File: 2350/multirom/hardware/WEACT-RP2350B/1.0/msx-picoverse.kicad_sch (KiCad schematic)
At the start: 9 parts, among them U1 WEACT-RP2350B

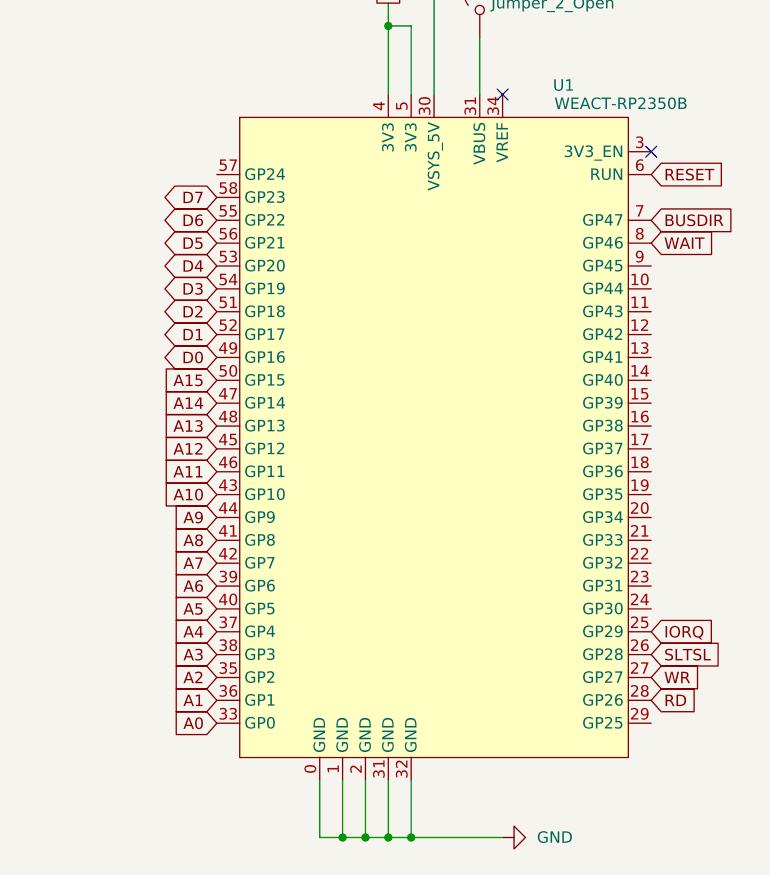
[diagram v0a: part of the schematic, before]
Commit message: loadrom and multirom ported to 2350
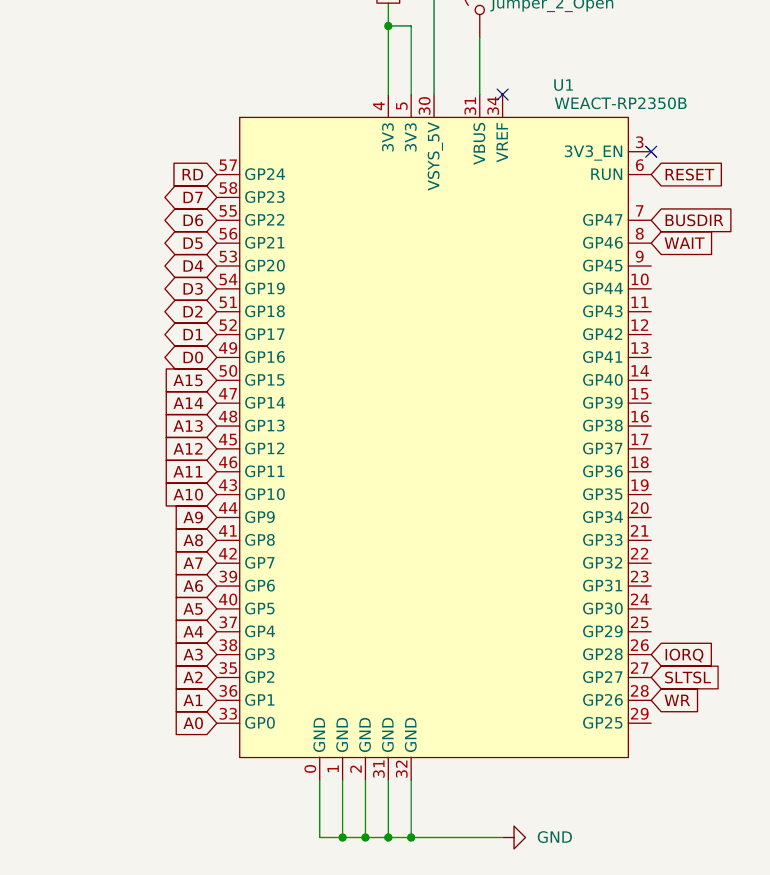
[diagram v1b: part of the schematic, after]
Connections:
- net IORQ: now also U1.26 (GP28); no longer U1.25 (GP29)
- net RD: now also U1.57 (GP24); no longer U1.28 (GP26)
- net SLTSL: now also U1.27 (GP27); no longer U1.26 (GP28)
- net WR: now also U1.28 (GP26); no longer U1.27 (GP27)

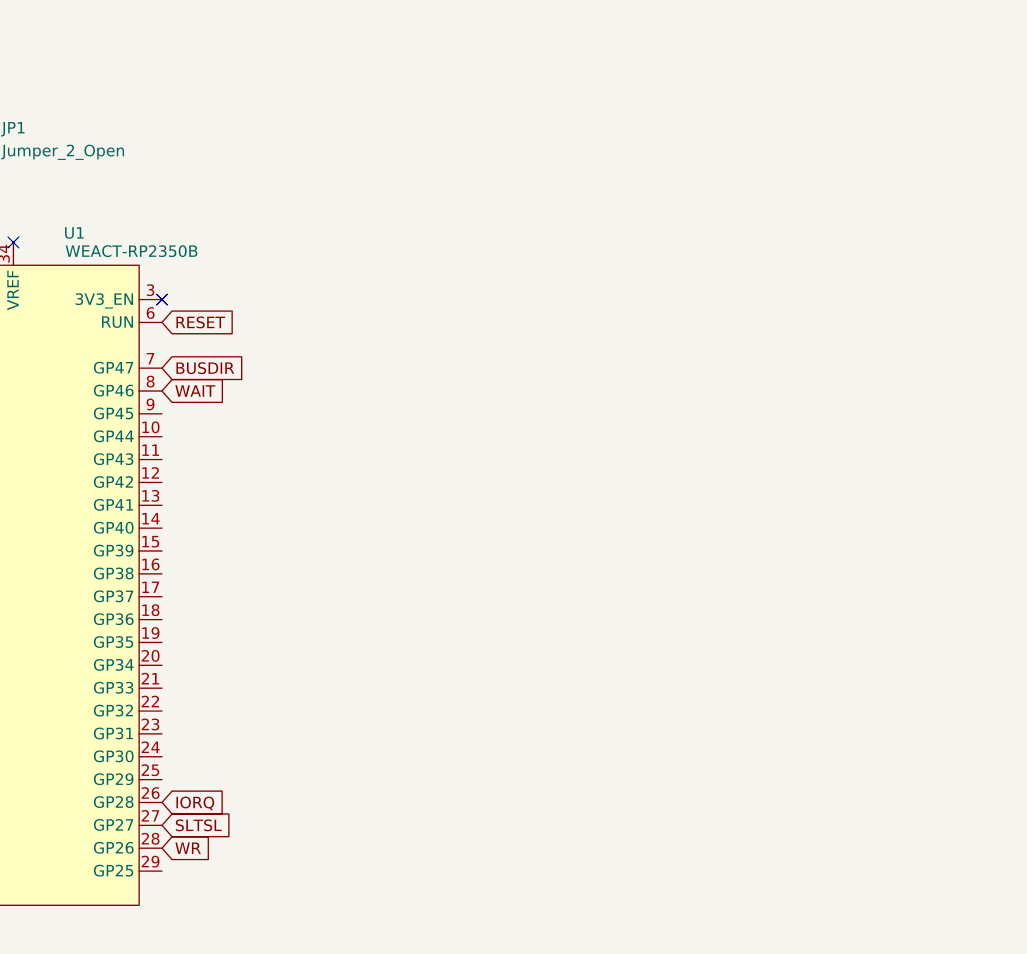
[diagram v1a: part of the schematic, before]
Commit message: connecting the microSD card
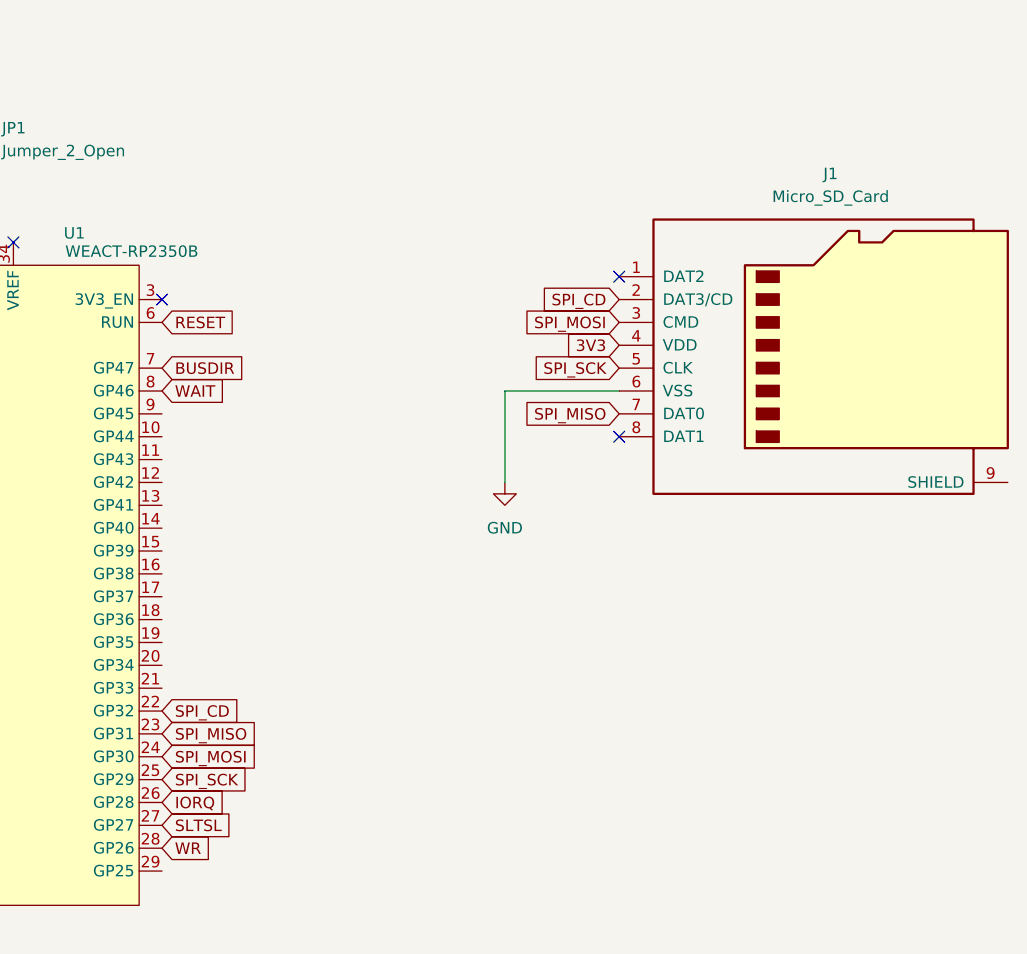
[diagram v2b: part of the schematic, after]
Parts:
- added J1: Micro_SD_Card, symbol Connector:Micro_SD_Card
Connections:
- net 3V3: now also J1.4 (VDD)
- net GND: now also J1.6 (VSS)
- net SPI_CD: now reaches U1.22 (GP32)
- net SPI_CD: now also J1.2 (DAT3/CD)
- net SPI_MISO: now reaches U1.23 (GP31)
- net SPI_MISO: now also J1.7 (DAT0)
- net SPI_MOSI: now reaches U1.24 (GP30)
- net SPI_MOSI: now also J1.3 (CMD)
- net SPI_SCK: now reaches U1.25 (GP29)
- net SPI_SCK: now also J1.5 (CLK)
- no-connect marks 15 -> 17

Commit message: playing with SPI libraries
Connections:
- net SPI_CD: now also U1.21 (GP33); no longer U1.22 (GP32)
- net SPI_MISO: now also U1.18 (GP36); no longer U1.23 (GP31)
- net SPI_MOSI: now also U1.19 (GP35); no longer U1.24 (GP30)
- net SPI_SCK: now also U1.20 (GP34); no longer U1.25 (GP29)
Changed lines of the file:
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@@
 	(global_label "SPI_SCK"
 		(shape input)
-		(at 297.18 127 0)
-		(fields_autoplaced yes)
-		(effects
-			(font
-				(size 1.27 1.27)
-			)
-			(justify left)
-		)
-		(property "Intersheetrefs" "${INTERSHEET_REFS}"
-			(at 307.9666 127 0)
-			(effects
-				(font
-					(size 1.27 1.27)
-				)
-				(justify left)
-				(hide yes)
-			)
-		)
-	)
-	(global_label "SPI_SCK"
-		(shape input)
 		(at 347.98 81.28 180)
 		(fields_autoplaced yes)
@@
 		)
 	)
+	(global_label "A3"
+		(shape input)
+		(at 248.92 129.54 180)
+		(fields_autoplaced yes)
+		(effects
+			(font
+				(size 1.27 1.27)
+			)
+			(justify right)
+		)
+		(property "Intersheetrefs" "${INTERSHEET_REFS}"
+			(at 243.6367 129.54 0)
+			(effects
+				(font
+					(size 1.27 1.27)
+				)
+				(justify right)
+				(hide yes)
+			)
+		)
+	)
 	(global_label "SPI_CD"
 		(shape input)
-		(at 297.18 119.38 0)
-		(fields_autoplaced yes)
-		(effects
-			(font
-				(size 1.27 1.27)
-			)
-			(justify left)
-		)
-		(property "Intersheetrefs" "${INTERSHEET_REFS}"
-			(at 306.7571 119.38 0)
-			(effects
-				(font
-					(size 1.27 1.27)
-				)
-				(justify left)
-				(hide yes)
-			)
-		)
-	)
-	(global_label "A3"
-		(shape input)
-		(at 248.92 129.54 180)
-		(fields_autoplaced yes)
-		(effects
-			(font
-				(size 1.27 1.27)
-			)
-			(justify right)
-		)
-		(property "Intersheetrefs" "${INTERSHEET_REFS}"
-			(at 243.6367 129.54 0)
-			(effects
-				(font
-					(size 1.27 1.27)
-				)
-				(justify right)
+		(at 297.18 116.84 0)
+		(fields_autoplaced yes)
+		(effects
+			(font
+				(size 1.27 1.27)
+			)
+			(justify left)
+		)
+		(property "Intersheetrefs" "${INTERSHEET_REFS}"
+			(at 306.7571 116.84 0)
+			(effects
+				(font
+					(size 1.27 1.27)
+				)
+				(justify left)
 				(hide yes)
 			)
@@
 		)
 	)
+	(global_label "SPI_MISO"
+		(shape input)
+		(at 297.18 109.22 0)
+		(fields_autoplaced yes)
+		(effects
+			(font
+				(size 1.27 1.27)
+			)
+			(justify left)
+		)
+		(property "Intersheetrefs" "${INTERSHEET_REFS}"
+			(at 308.8133 109.22 0)
+			(effects
+				(font
+					(size 1.27 1.27)
+				)
+				(justify left)
+				(hide yes)
+			)
+		)
+	)
 	(global_label "RD"
 		(shape input)
@@
 		)
 	)
+	(global_label "SPI_SCK"
+		(shape input)
+		(at 297.18 114.3 0)
+		(fields_autoplaced yes)
+		(effects
+			(font
+				(size 1.27 1.27)
+			)
+			(justify left)
+		)
+		(property "Intersheetrefs" "${INTERSHEET_REFS}"
+			(at 307.9666 114.3 0)
+			(effects
+				(font
+					(size 1.27 1.27)
+				)
+				(justify left)
+				(hide yes)
+			)
+		)
+	)
 	(global_label "A10"
 		(shape input)
@@
 				)
 				(justify right)
+				(hide yes)
+			)
+		)
+	)
+	(global_label "SPI_MOSI"
+		(shape input)
+		(at 297.18 111.76 0)
+		(fields_autoplaced yes)
+		(effects
+			(font
+				(size 1.27 1.27)
+			)
+			(justify left)
+		)
+		(property "Intersheetrefs" "${INTERSHEET_REFS}"
+			(at 308.8133 111.76 0)
+			(effects
+				(font
+					(size 1.27 1.27)
+				)
+				(justify left)
 				(hide yes)
 			)
@@
 		)
 	)
-	(global_label "SPI_MOSI"
-		(shape input)
-		(at 297.18 124.46 0)
-		(fields_autoplaced yes)
-		(effects
-			(font
-				(size 1.27 1.27)
-			)
-			(justify left)
-		)
-		(property "Intersheetrefs" "${INTERSHEET_REFS}"
-			(at 308.8133 124.46 0)
-			(effects
-				(font
-					(size 1.27 1.27)
-				)
-				(justify left)
-				(hide yes)
-			)
-		)
-	)
 	(global_label "WR"
 		(shape input)
@@
 			(effects
 				(font
-					(size 1.27 1.27)
-				)
-				(justify left)
-				(hide yes)
-			)
-		)
-	)
-	(global_label "SPI_MISO"
-		(shape input)
-		(at 297.18 121.92 0)
-		(fields_autoplaced yes)
-		(effects
-			(font
-				(size 1.27 1.27)
-			)
-			(justify left)
-		)
-		(property "Intersheetrefs" "${INTERSHEET_REFS}"
-			(at 308.8133 121.92 0)
-			(effects
-				(font
